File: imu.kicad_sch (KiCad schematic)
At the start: 11 parts, among them J3 IMU_FFC_Conn, U6 LSM6DSLTR

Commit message: On production | V0.1
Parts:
- removed D4: LED_BLUE, LED_SMD:LED_0603_1608Metric, symbol Device:LED
- removed R18: 1k, Resistor_SMD:R_0402_1005Metric, symbol Device:R
- added 3V1, CS1, GND1, INT1, MISO1, MOSI1, SCK1: ~, TestPoint:TestPoint_Pad_D2.0mm, symbol Connector:TestPoint
- added R18 (x2): 47, Resistor_SMD:R_0402_1005Metric, symbol Device:R
- H1, H2: symbol Mechanical:MountingHole -> Mechanical:MountingHole_Pad; now left out of the parts list
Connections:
- net 3V3: now also 3V1.1
- net CS: now also D9.4 (K), CS1.1; no longer D9.6 (K)
- net GND2: now also GND1.1
- net INT1: now also INT1.1, R18.1; no longer U6.4 (INT1)
- net MISO: now also D9.6 (K), MISO1.1, R18.2; no longer D9.3 (K), U6.1 (SDO/SA0)
- net MOSi: now also D9.3 (K), MOSI1.1; no longer D9.4 (K)
- net SCK: now also SCK1.1
- new net: R18.1, U6.1 (SDO/SA0)
- new net: R18.2, U6.4 (INT1)
- new net Earth_Protective: H1.1, H2.1
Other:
- note added: "CONNECTORS"
- note removed: "CONNECTOR"
- moved on the sheet: D4, J3, R19

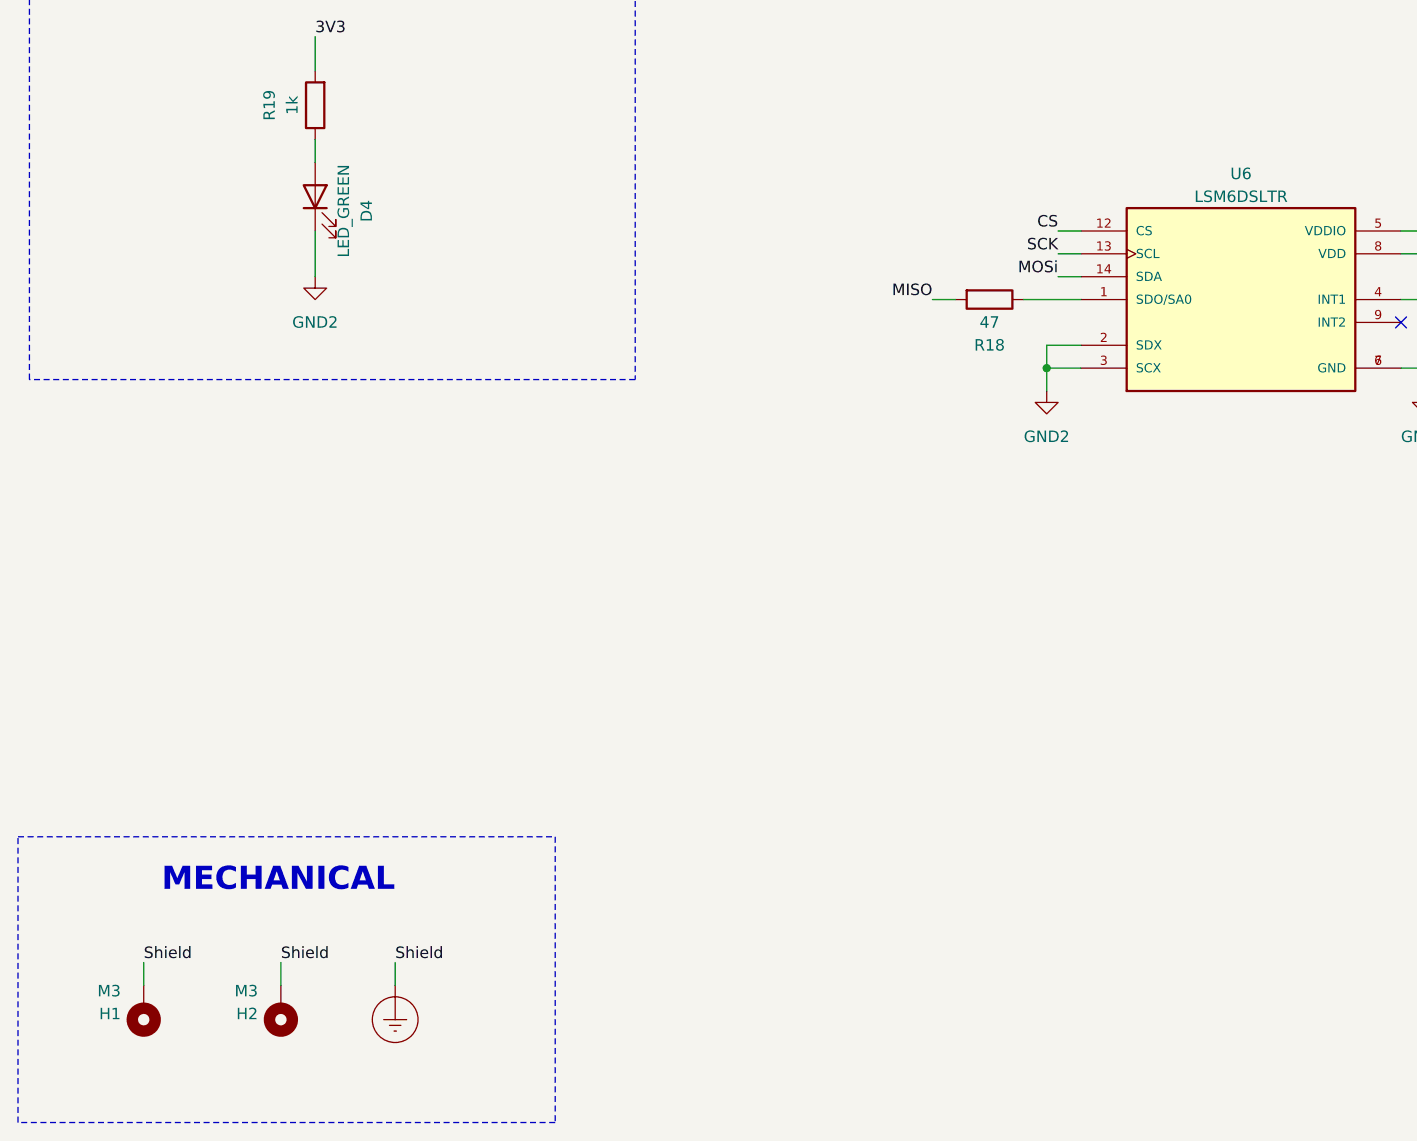
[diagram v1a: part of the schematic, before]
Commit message: Add hysteresis to IR sensor. Update README file.
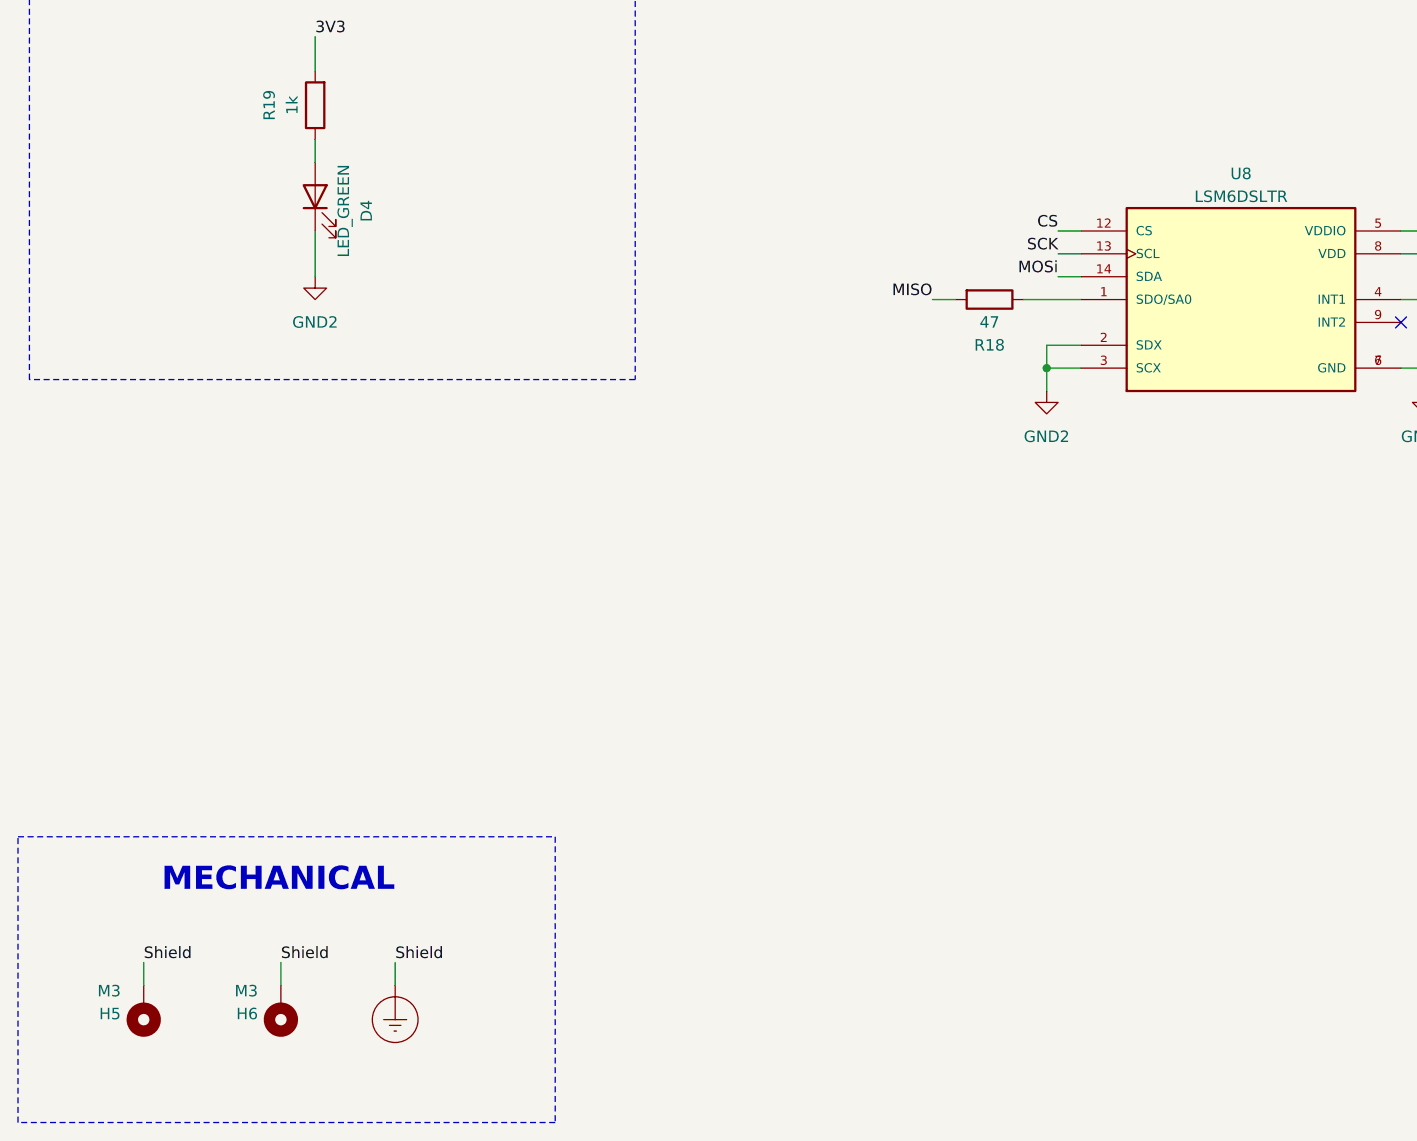
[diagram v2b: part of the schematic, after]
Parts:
- C2: footprint Capacitor_SMD:C_01005_0402Metric -> Capacitor_SMD:C_0402_1005Metric
- D9: footprint Package_TO_SOT_SMD:SOT-23-6 -> Package_TO_SOT_SMD:SOT-363_SC-70-6
- renumbered H1 to H5, H2 to H6, U6 to U8
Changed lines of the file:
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@@
   (symbol (lib_id "power:Earth_Protective") (at 54.61 181.61 0) (unit 1)
     (in_bom yes) (on_board yes) (dnp no) (fields_autoplaced)
-    (property "Reference" "#PWR03" (at 60.96 187.96 0)
+    (property "Reference" "#PWR075" (at 60.96 187.96 0)
       (effects (font (size 1.27 1.27)) hide)
     )
@@
   (symbol (lib_id "power:GND2") (at 168.91 115.57 0) (unit 1)
     (in_bom yes) (on_board yes) (dnp no) (fields_autoplaced)
-    (property "Reference" "#PWR068" (at 168.91 121.92 0)
+    (property "Reference" "#PWR079" (at 168.91 121.92 0)
       (effects (font (size 1.27 1.27)) hide)
     )
@@
   (symbol (lib_id "LSM6DSLTR:LSM6DSLTR") (at 148.59 105.41 0) (unit 1)
     (in_bom yes) (on_board yes) (dnp no) (fields_autoplaced)
-    (property "Reference" "U6" (at 148.59 91.44 0)
+    (property "Reference" "U8" (at 148.59 91.44 0)
       (effects (font (size 1.27 1.27)))
     )
@@
   (symbol (lib_id "power:GND2") (at 102.87 48.26 0) (unit 1)
     (in_bom yes) (on_board yes) (dnp no) (fields_autoplaced)
-    (property "Reference" "#PWR078" (at 102.87 54.61 0)
+    (property "Reference" "#PWR077" (at 102.87 54.61 0)
       (effects (font (size 1.27 1.27)) hide)
     )
@@
   (symbol (lib_id "Mechanical:MountingHole_Pad") (at 26.67 184.15 180) (unit 1)
     (in_bom no) (on_board yes) (dnp no) (fields_autoplaced)
-    (property "Reference" "H1" (at 24.13 184.785 0)
+    (property "Reference" "H5" (at 24.13 184.785 0)
       (effects (font (size 1.27 1.27)) (justify left))
     )
@@
   (symbol (lib_id "power:GND2") (at 57.15 43.18 0) (unit 1)
     (in_bom yes) (on_board yes) (dnp no) (fields_autoplaced)
-    (property "Reference" "#PWR072" (at 57.15 49.53 0)
+    (property "Reference" "#PWR076" (at 57.15 49.53 0)
       (effects (font (size 1.27 1.27)) hide)
     )
@@
       (effects (font (size 1.27 1.27)) (justify left))
     )
-    (property "Footprint" "Capacitor_SMD:C_01005_0402Metric" (at 36.5252 41.91 0)
+    (property "Footprint" "Capacitor_SMD:C_0402_1005Metric" (at 36.5252 41.91 0)
       (effects (font (size 1.27 1.27)) hide)
     )
@@
       (effects (font (size 1.27 1.27)) (justify left))
     )
-    (property "Footprint" "Capacitor_SMD:C_01005_0402Metric" (at 58.1152 41.91 0)
+    (property "Footprint" "Capacitor_SMD:C_0402_1005Metric" (at 58.1152 41.91 0)
       (effects (font (size 1.27 1.27)) hide)
     )
@@
   (symbol (lib_id "power:GND2") (at 35.56 43.18 0) (unit 1)
     (in_bom yes) (on_board yes) (dnp no) (fields_autoplaced)
-    (property "Reference" "#PWR071" (at 35.56 49.53 0)
+    (property "Reference" "#PWR073" (at 35.56 49.53 0)
       (effects (font (size 1.27 1.27)) hide)
     )
@@
   (symbol (lib_id "power:GND2") (at 127 115.57 0) (unit 1)
     (in_bom yes) (on_board yes) (dnp no) (fields_autoplaced)
-    (property "Reference" "#PWR074" (at 127 121.92 0)
+    (property "Reference" "#PWR078" (at 127 121.92 0)
       (effects (font (size 1.27 1.27)) hide)
     )
@@
   (symbol (lib_id "Mechanical:MountingHole_Pad") (at 41.91 184.15 180) (unit 1)
     (in_bom no) (on_board yes) (dnp no) (fields_autoplaced)
-    (property "Reference" "H2" (at 39.37 184.785 0)
+    (property "Reference" "H6" (at 39.37 184.785 0)
       (effects (font (size 1.27 1.27)) (justify left))
     )
@@
   (symbol (lib_id "power:GND2") (at 243.84 44.45 0) (unit 1)
     (in_bom yes) (on_board yes) (dnp no) (fields_autoplaced)
-    (property "Reference" "#PWR067" (at 243.84 50.8 0)
+    (property "Reference" "#PWR081" (at 243.84 50.8 0)
       (effects (font (size 1.27 1.27)) hide)
     )
@@
   (symbol (lib_id "power:GND2") (at 171.45 49.53 0) (unit 1)
     (in_bom yes) (on_board yes) (dnp no) (fields_autoplaced)
-    (property "Reference" "#PWR078" (at 171.45 55.88 0)
+    (property "Reference" "#PWR080" (at 171.45 55.88 0)
       (effects (font (size 1.27 1.27)) hide)
     )
@@
   (symbol (lib_id "power:GND2") (at 45.72 102.87 0) (unit 1)
     (in_bom yes) (on_board yes) (dnp no) (fields_autoplaced)
-    (property "Reference" "#PWR075" (at 45.72 109.22 0)
+    (property "Reference" "#PWR074" (at 45.72 109.22 0)
       (effects (font (size 1.27 1.27)) hide)
     )
@@
       (effects (font (size 1.27 1.27)))
     )
-    (property "Footprint" "Package_TO_SOT_SMD:SOT-23-6" (at 251.46 49.53 0)
+    (property "Footprint" "Package_TO_SOT_SMD:SOT-363_SC-70-6" (at 251.46 49.53 0)
       (effects (font (size 1.27 1.27)) (justify left) hide)
     )
